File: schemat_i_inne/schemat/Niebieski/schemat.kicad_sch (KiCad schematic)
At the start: 36 parts, among them J5 programming port, J6 USB_B_Micro, SW1 SW_DIP_x01, SW2 Home, SW3 triggerR, SW4 Select, SW5 triggerL, SW6 BumperL, SW7 BumperR, U1 ATmega1284P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

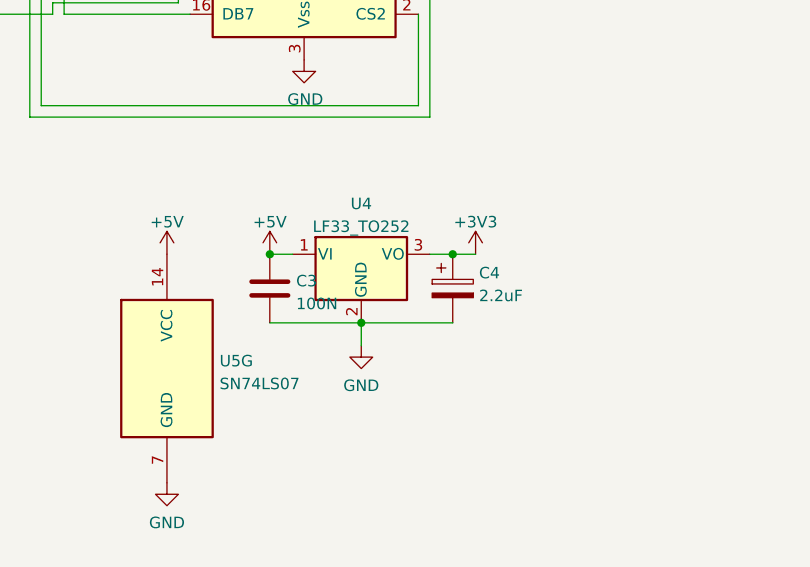
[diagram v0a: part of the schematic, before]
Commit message: Footprint for joysticks corrected
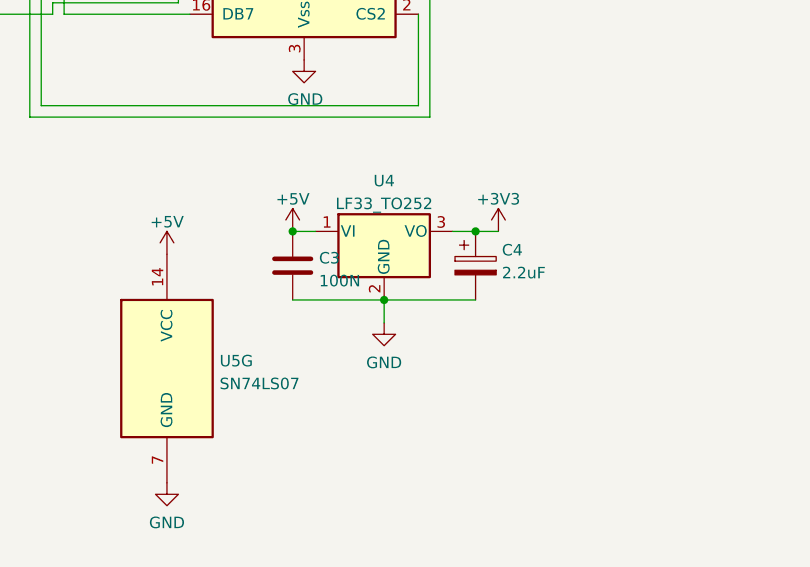
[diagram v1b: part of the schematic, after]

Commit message: More footprints updated - buttons - USB micro - coil
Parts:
- J6: footprint USB:microUSB -> Connector_USB:USB_Micro-B_Amphenol_10104110_Horizontal
- L1: footprint Inductor_SMD:L_6.3x6.3_H3 -> Inductor_SMD:L_Bourns-SRN4018
- RV1: footprint Potentiometer_THT:Potentiometer_Bourns_3296Z_Horizontal -> Blue:potentiometer10K
- SW2, SW4: footprint Button_Switch_SMD:SW_Push_1P1T_NO_6x6mm_H9.5mm -> buttons:buttonSMD_withHoles
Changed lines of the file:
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@@
       (effects (font (size 1.27 1.27)))
     )
-    (property "Footprint" "Potentiometer_THT:Potentiometer_Bourns_3296Z_Horizontal" (at 167.64 107.95 0)
+    (property "Footprint" "Blue:potentiometer10K" (at 167.64 107.95 0)
       (effects (font (size 1.27 1.27)) hide)
     )
@@
       (effects (font (size 1.27 1.27)) (justify left))
     )
-    (property "Footprint" "USB:microUSB" (at 105.41 177.8 0)
+    (property "Footprint" "Connector_USB:USB_Micro-B_Amphenol_10104110_Horizontal" (at 105.41 177.8 0)
       (effects (font (size 1.27 1.27)) hide)
     )
@@
       (effects (font (size 1.27 1.27)))
     )
-    (property "Footprint" "Button_Switch_SMD:SW_Push_1P1T_NO_6x6mm_H9.5mm" (at 74.93 74.93 0)
+    (property "Footprint" "buttons:buttonSMD_withHoles" (at 74.93 74.93 0)
       (effects (font (size 1.27 1.27)) hide)
     )
@@
       (effects (font (size 1.27 1.27)))
     )
-    (property "Footprint" "Button_Switch_SMD:SW_Push_1P1T_NO_6x6mm_H9.5mm" (at 54.61 127 0)
+    (property "Footprint" "buttons:buttonSMD_withHoles" (at 54.61 127 0)
       (effects (font (size 1.27 1.27)) hide)
     )
@@
       (effects (font (size 1.27 1.27)) (justify left))
     )
-    (property "Footprint" "Inductor_SMD:L_6.3x6.3_H3" (at 101.6 40.64 0)
-      (effects (font (size 1.27 1.27)) hide)
-    )
+    (property "Footprint" "Inductor_SMD:L_Bourns-SRN4018" (at 101.6 40.64 0)
+      (effects (font (size 1.27 1.27)) hide)
+    )

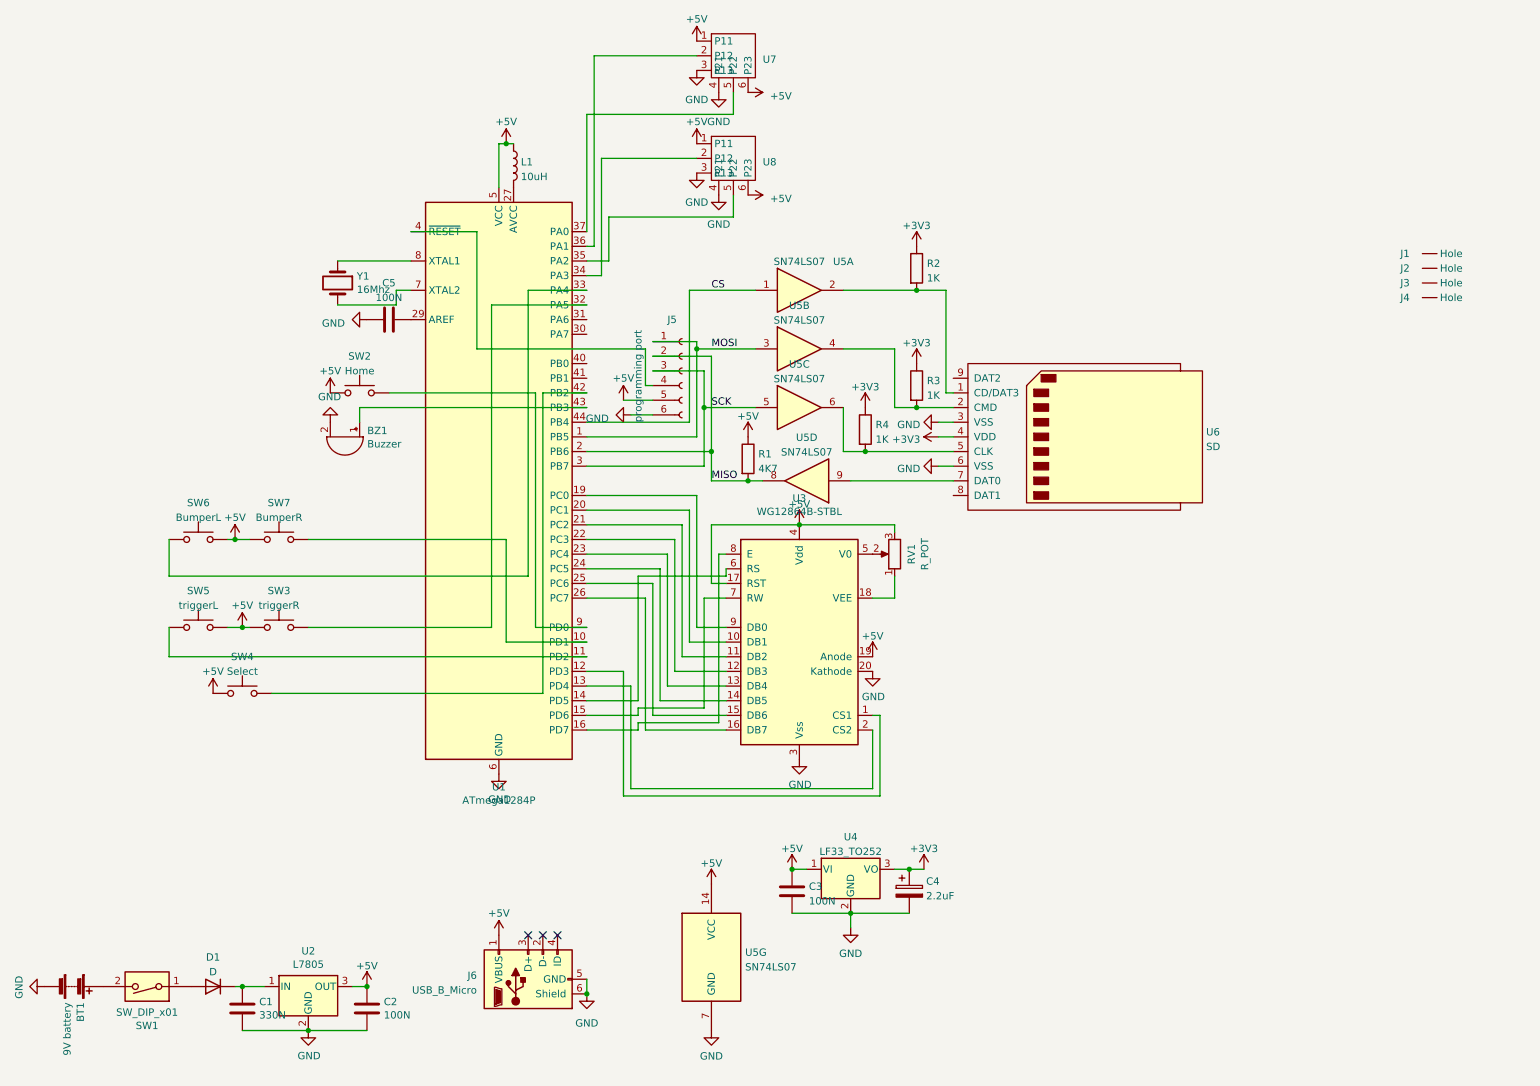
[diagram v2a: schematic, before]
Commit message: Fully updated PCB of RetCon
- It is in schemat/Niebieski folder
- First checkout of parts has been done
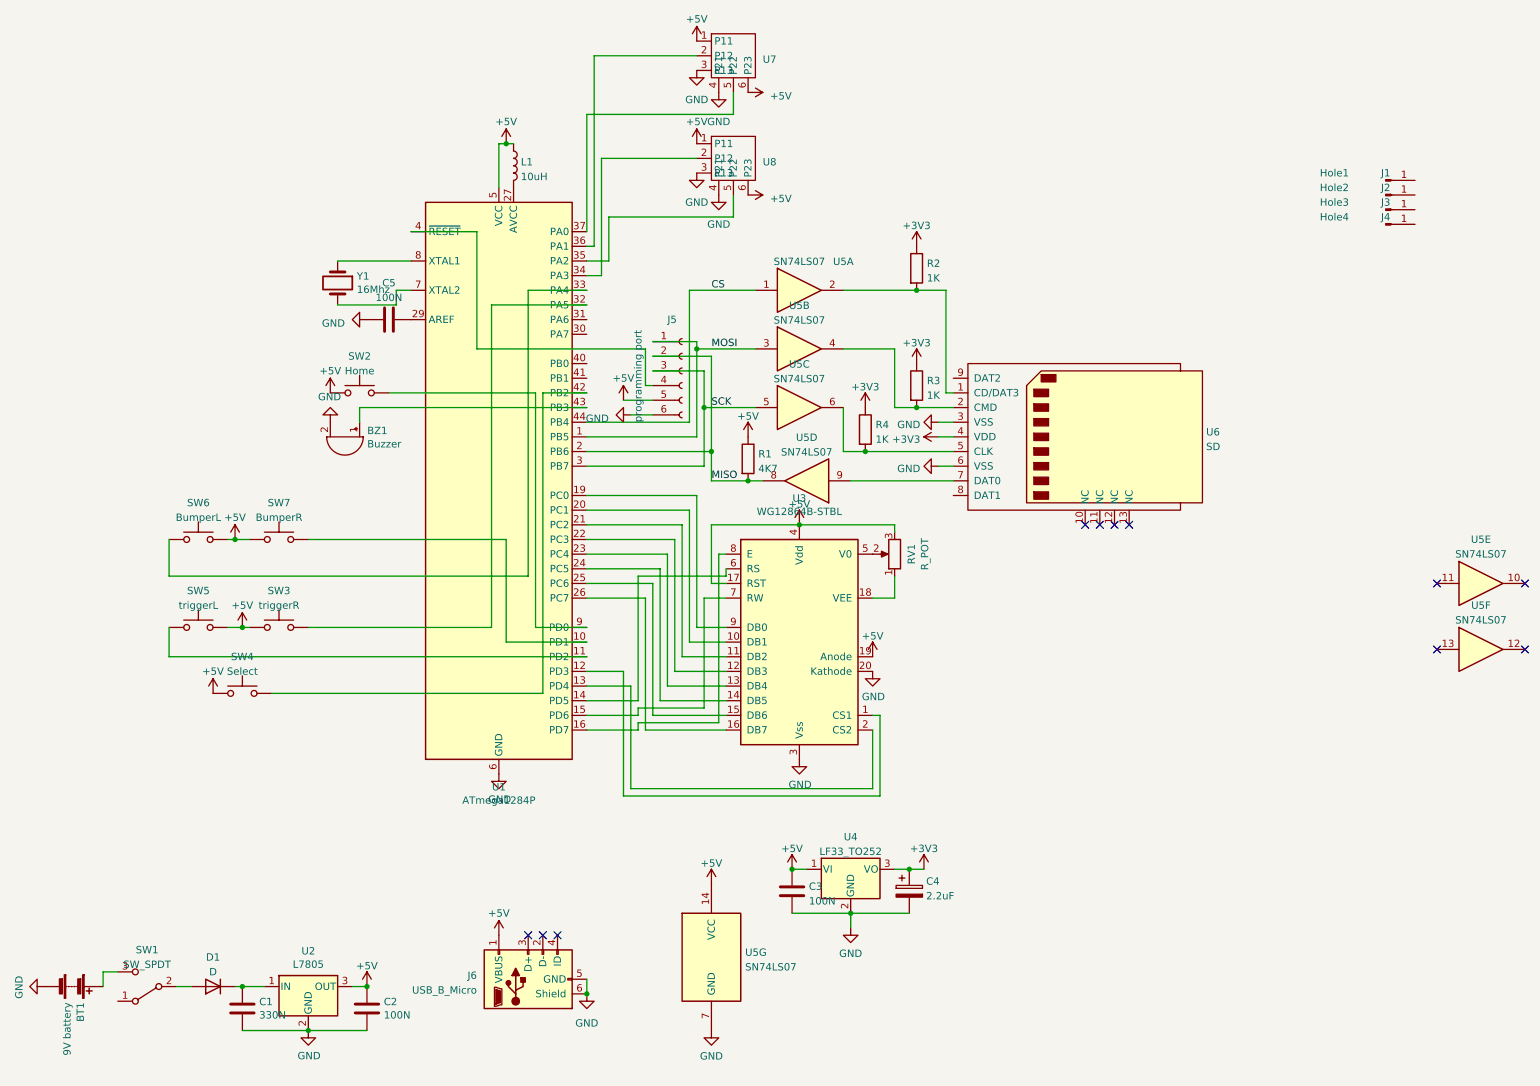
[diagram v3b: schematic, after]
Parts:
- removed J1, J2, J3, J4: ~, Holes:One_hole, symbol Holes:One_hole
- removed SW1: SW_DIP_x01, Button_Switch_SMD:SW_DIP_SPSTx01_Slide_Copal_CVS-01xB_W5.9mm_P1mm, symbol Switch:SW_DIP_x01
- added J1: Hole1, Holes:One_hole, symbol Connector:Conn_01x01_Pin
- added J2: Hole2, Holes:One_hole, symbol Connector:Conn_01x01_Pin
- added J3: Hole3, Holes:One_hole, symbol Connector:Conn_01x01_Pin
- added J4: Hole4, Holes:One_hole, symbol Connector:Conn_01x01_Pin
- added SW1: SW_SPDT, buttons:Button_Switch, symbol Switch:SW_SPDT
- added unit 6 of U5
- added unit 5 of U5
- C4: footprint Capacitor_SMD:CP_Elec_6.3x5.4_Nichicon -> Capacitor_SMD:C_1206_3216Metric
- J6: footprint Connector_USB:USB_Micro-B_Amphenol_10104110_Horizontal -> USB:USBMicro-SMD
- U6: symbol SD:SD -> sd:SD
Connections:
- net at D1.2 (A): now also SW1.2 (B)
- net at BT1.1 (+): now also SW1.3 (C)
- no-connect marks 3 -> 11
